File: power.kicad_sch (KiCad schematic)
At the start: 68 parts, among them J24 PWR IN, J25 PWR PROT, J26 PWR 3.3V, J27 SAFING, J28 ARM, J29 ACT HOT, J30 ACT COLD, K1 J115F11C, Q1 SI7220 NMOS, Q2 NMOS, U34 TLI4971, U35 LTC4367, U36 ADS1110, U37 AP64350, U38 TLP241A, U39 LP5912-3.3DRV

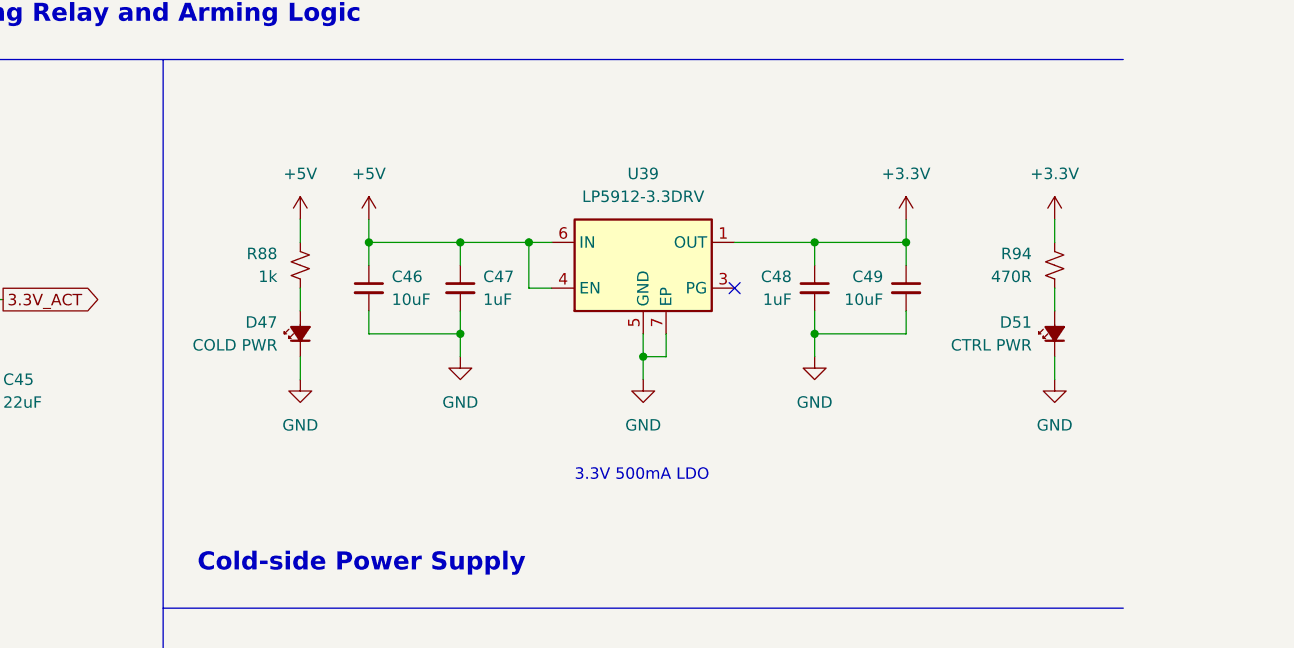
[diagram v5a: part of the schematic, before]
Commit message: Group components
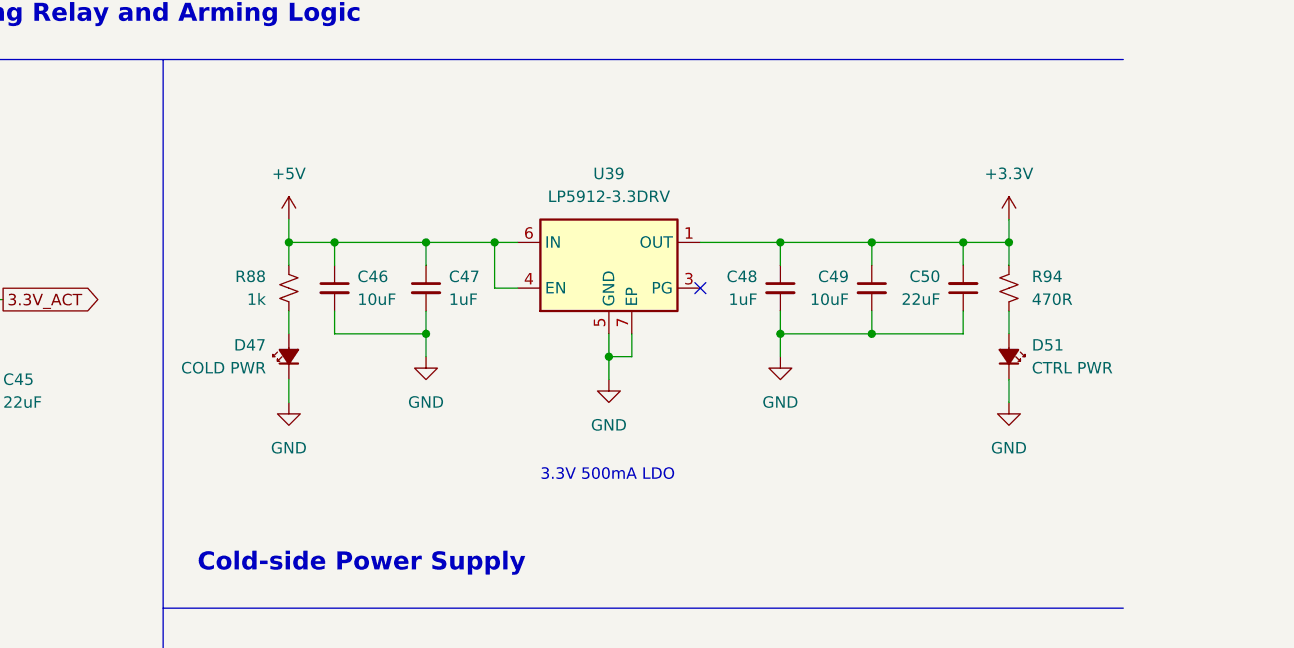
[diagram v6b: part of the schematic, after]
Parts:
- added C50: 22uF, Capacitor_SMD:C_1206_3216Metric, symbol Device:C_Small
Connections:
- net +3.3V: now also C50.2
- net GND: now also C50.1
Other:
- moved on the sheet: C46, C47, C48, C49, D47, D51, R88, R94, U39

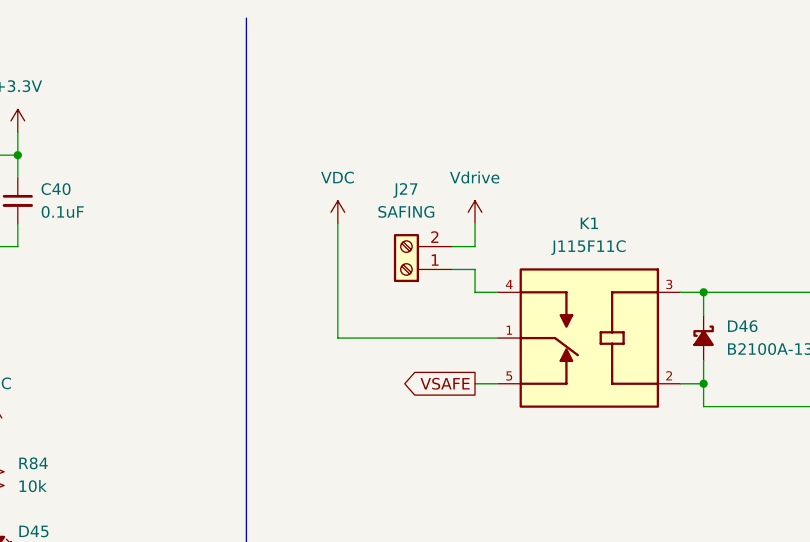
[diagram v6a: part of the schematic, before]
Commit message: Modified de-safing key arrangement
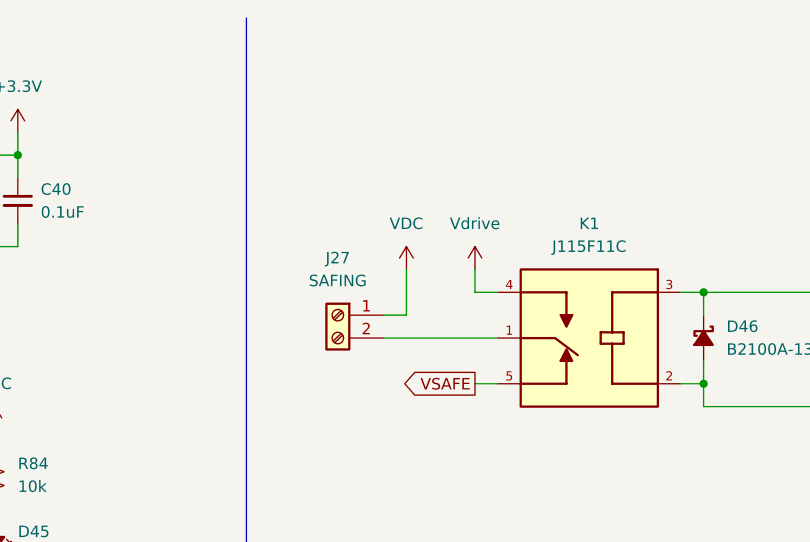
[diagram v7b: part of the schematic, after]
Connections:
- net VDC: now also J27.1 (Pin_1); no longer K1.1
- net Vdrive: now also K1.4; no longer J27.2 (Pin_2)
- new net: J27.2 (Pin_2), K1.1
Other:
- moved on the sheet: J27

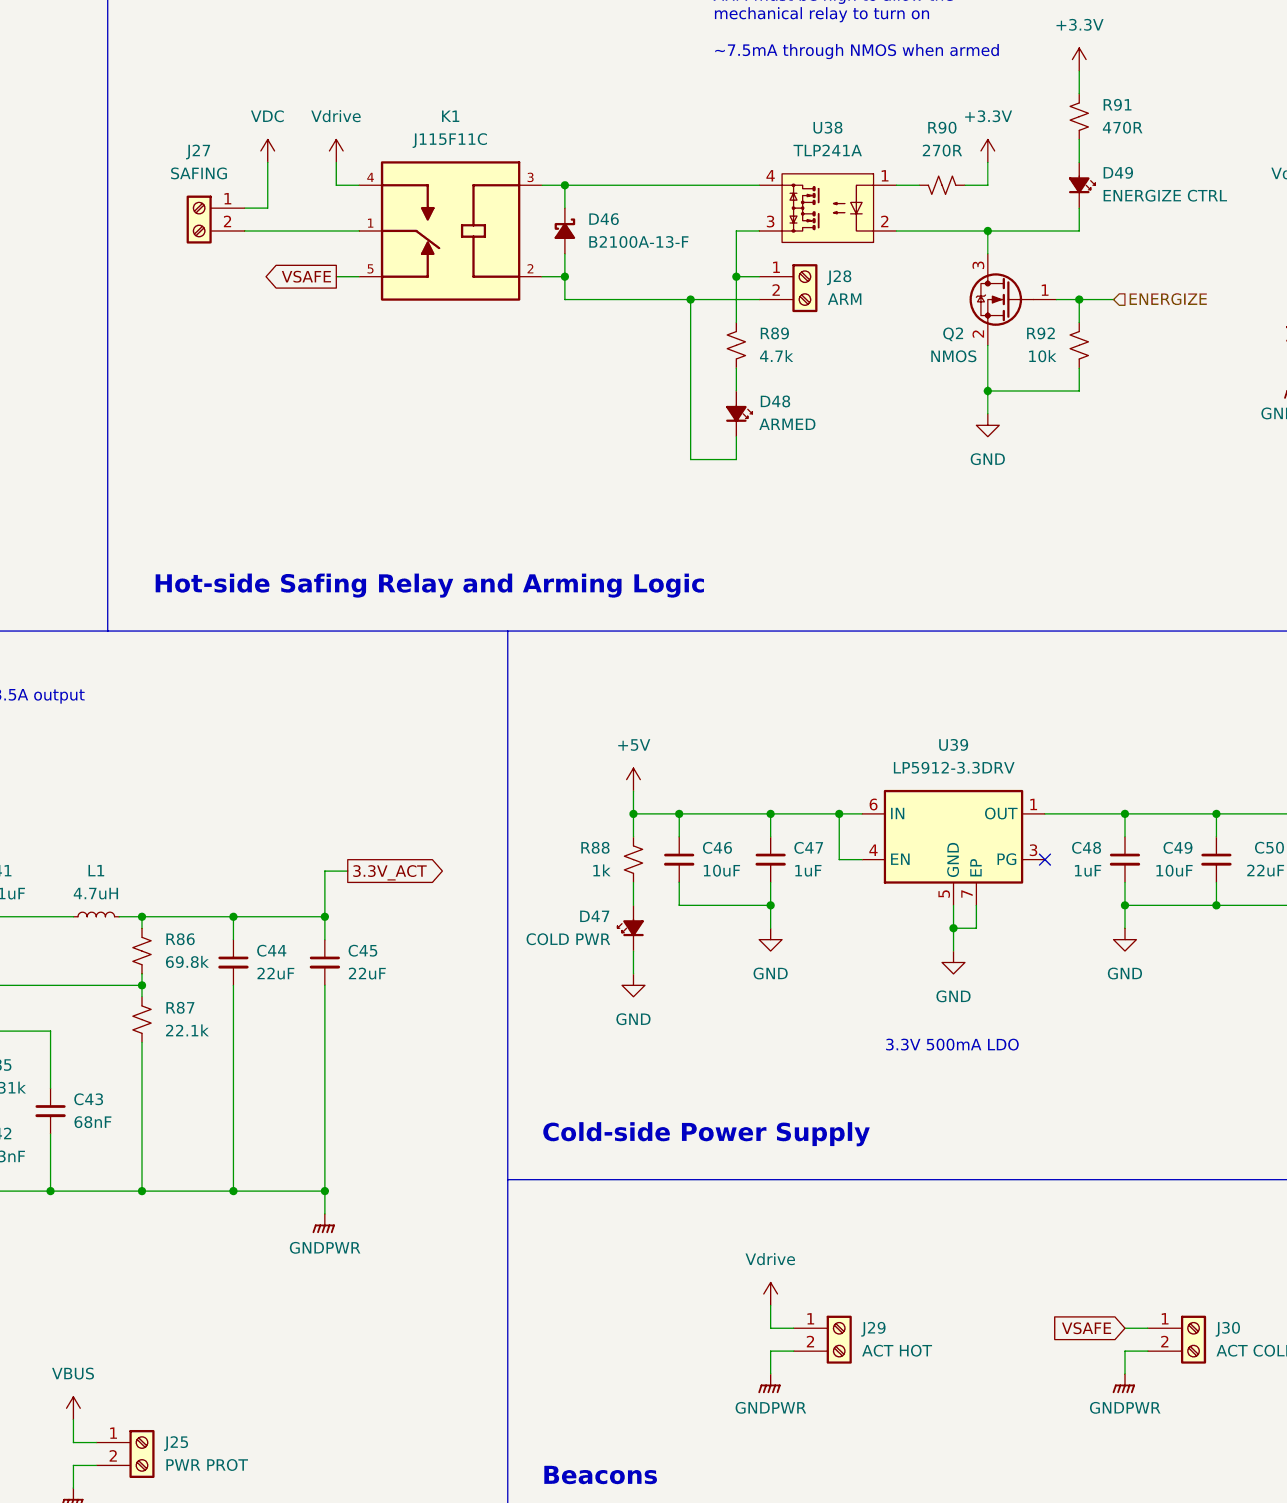
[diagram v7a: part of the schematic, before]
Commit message: Check-safe channel, footprint changes
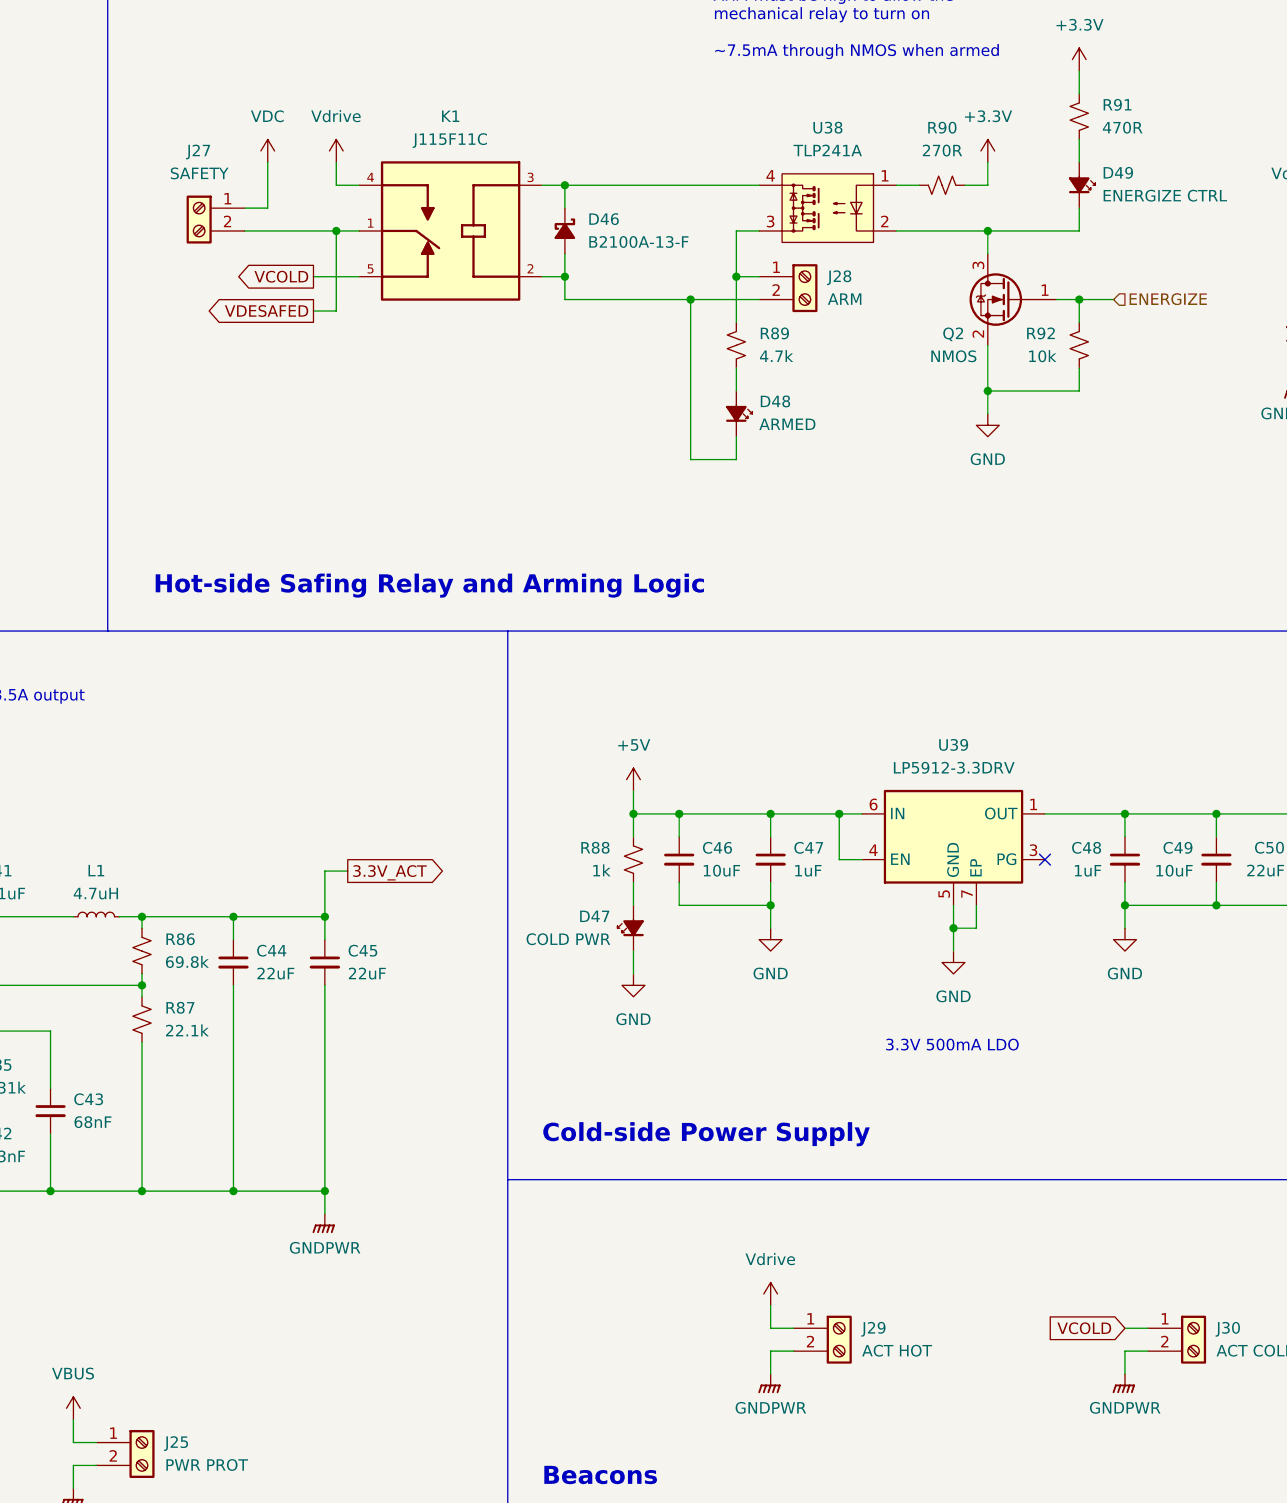
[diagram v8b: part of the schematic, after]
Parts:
- J24: footprint actuation:1773976 -> actuation:XT90PW-M; MPN 1773976 -> XT90PW-M
- J25, J26, J29, J30: footprint actuation:1989447 -> Connector_AMASS:AMASS_XT60-M_1x02_P7.20mm_Vertical; MPN 1989447 -> XT60-M
- J27: value SAFING -> SAFETY; footprint actuation:1773976 -> actuation:XT90PW-M; MPN 1773976 -> XT90PW-M
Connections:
- net VDESAFED: now reaches J27.2 (Pin_2), K1.1
- net VSAFE renamed VCOLD
